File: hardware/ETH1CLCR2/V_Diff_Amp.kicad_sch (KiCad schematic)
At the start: 83 parts, among them K801 TQ2SA-5V, Q801 BC847, U801 MCP6L91T-E/SN, U802 MCP661-E/SN, U803 MCP661-E/SN, U804 SN74LVC1G3157DBVR, U805 SN74LVC1G3157DBVR, U806 MCP661-E/SN, U807 MCP6L91T-E/SN, U808 MCP661-E/SN, U809 SN74LVC1T45DBV, U810 SN74LVC1G3157DBVR, U811 SN74LVC1G3157DBVR, U812 MCP661-E/SN, U813 MCP6L91T-E/SN, U814 SN74LVC1T45DBV, U815 SN74LVC1T45DBV

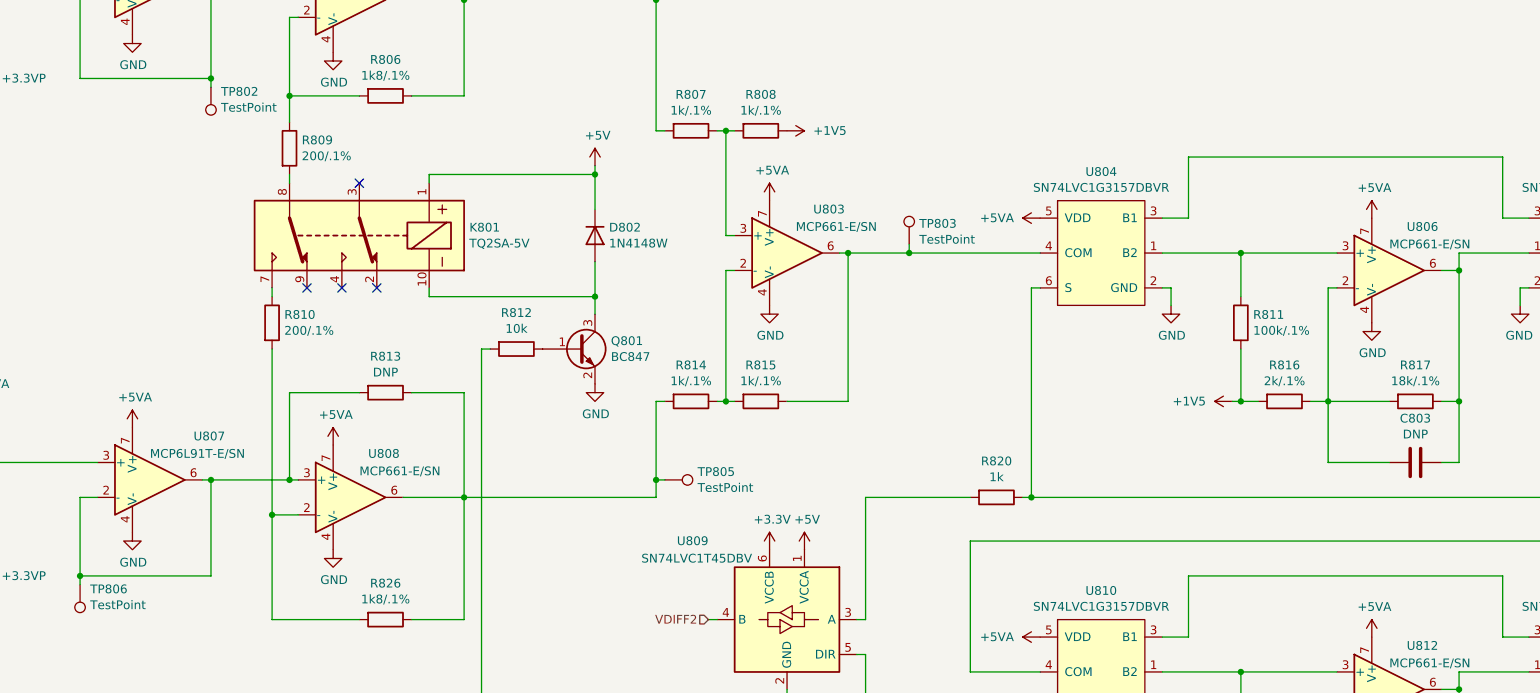
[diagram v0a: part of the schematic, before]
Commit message: Added text to schematics, software development.
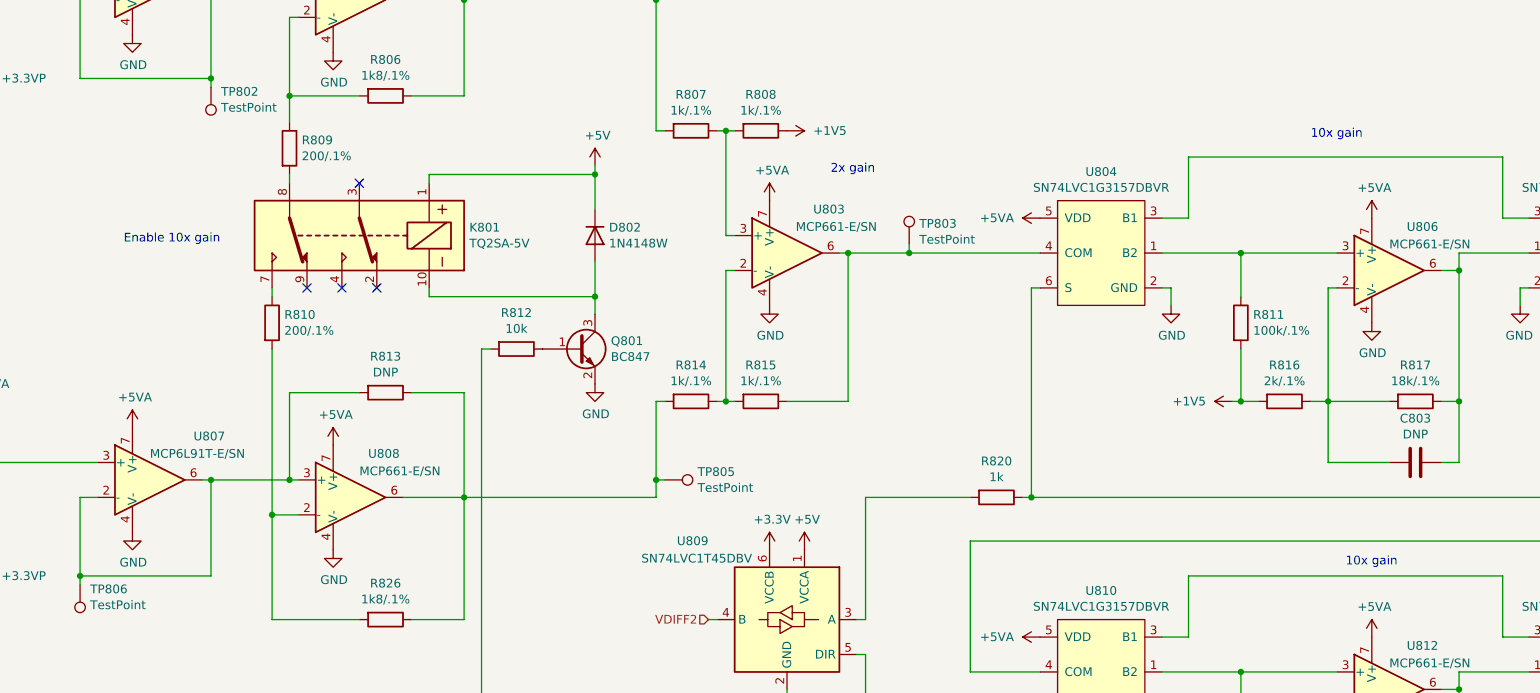
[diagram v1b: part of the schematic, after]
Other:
- note added: "10x gain"
- note added: "2x gain"
- note added: "Enable 10x gain"
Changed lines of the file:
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@@
     (stroke (width 0) (type default) (color 0 0 0 0))
+  )
+  (text "Enable 10x gain" (at 82.55 93.98 0)
+    (effects (font (size 1.27 1.27)) (justify left bottom))
+  )
+  (text "10x gain" (at 260.35 140.97 0)
+    (effects (font (size 1.27 1.27)) (justify left bottom))
+  )
+  (text "10x gain" (at 255.27 78.74 0)
+    (effects (font (size 1.27 1.27)) (justify left bottom))
+  )
+  (text "2x gain" (at 185.42 83.82 0)
+    (effects (font (size 1.27 1.27)) (justify left bottom))
   )
   (hierarchical_label "L_POT" (shape input) (at 25.4 125.73 180)

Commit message: Software development
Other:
- note added: "Delete K801"
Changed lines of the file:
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@@
+    (effects (font (size 1.27 1.27)) (justify left bottom))
+  )
+  (text "Delete K801" (at 85.09 97.79 0)
     (effects (font (size 1.27 1.27)) (justify left bottom))
   )
